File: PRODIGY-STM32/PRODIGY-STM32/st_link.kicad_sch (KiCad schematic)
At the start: 33 parts, among them J3 Conn_ARM_JTAG_SWD_10, Q1 BC850, U1 AP2112K-3.3, U2 STM32F103C8Tx, Y1 8MHz

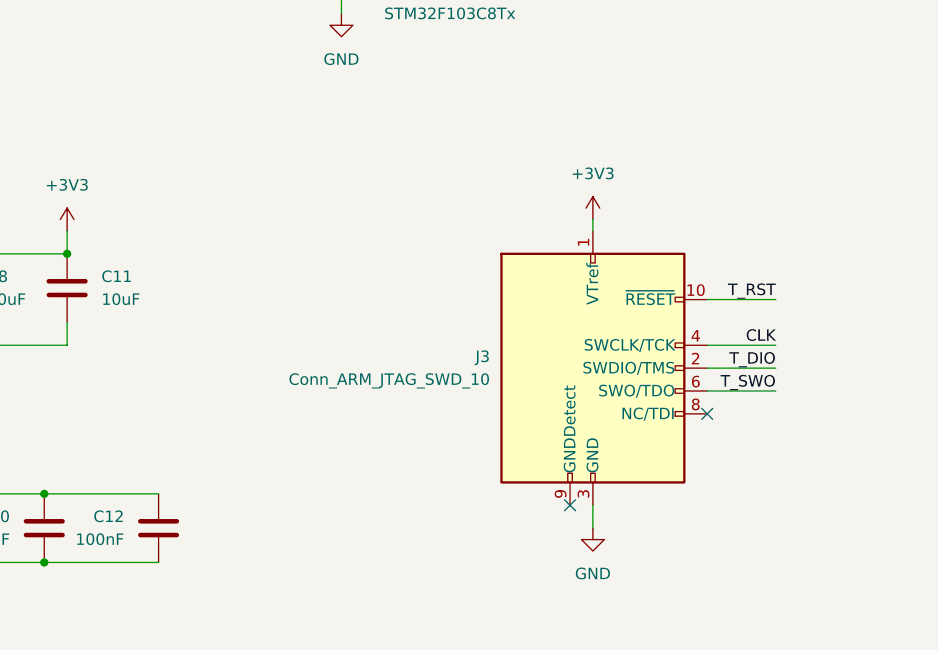
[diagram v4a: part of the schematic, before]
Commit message: stm32 layout done, schematic swd coinnector updated
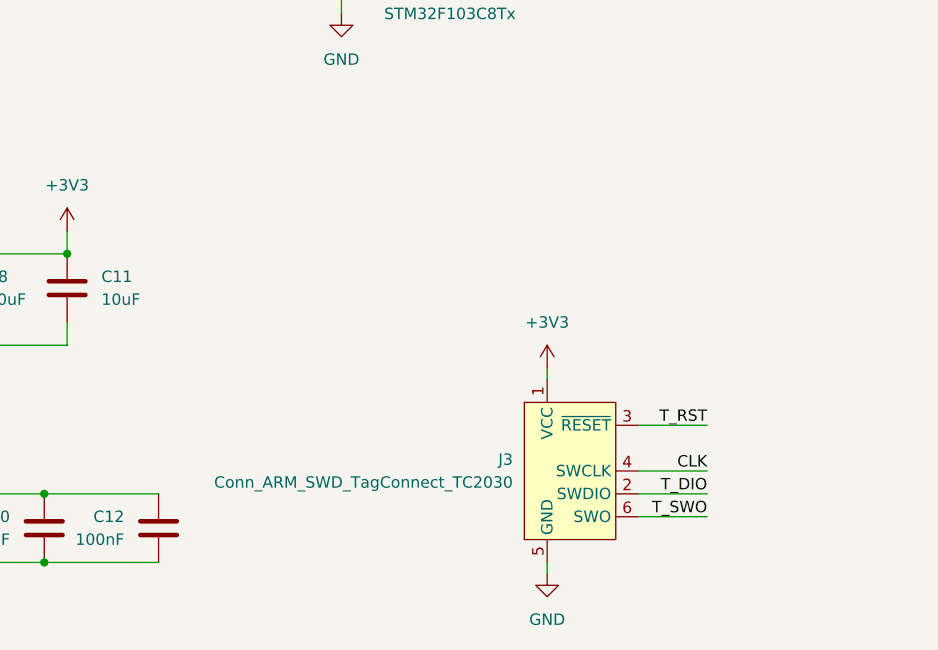
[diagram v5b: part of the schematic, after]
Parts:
- removed J3: Conn_ARM_JTAG_SWD_10, Connector_IDC:IDC-Header_2x05_P2.54mm_Vertical, symbol Connector:Conn_ARM_JTAG_SWD_10
- added J3: Conn_ARM_SWD_TagConnect_TC2030, Connector_PinHeader_2.54mm:PinHeader_1x06_P2.54mm_Vertical, symbol Connector:Conn_ARM_SWD_TagConnect_TC2030
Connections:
- net +3V3: now also J3.1 (VCC)
- net CLK: now also J3.4 (SWCLK)
- net GND: now also J3.5 (GND)
- net T_DIO: now also J3.2 (SWDIO)
- net T_RST: now also J3.3 (~{RESET})
- net T_SWO: now also J3.6 (SWO)
- no-connect marks 20 -> 18

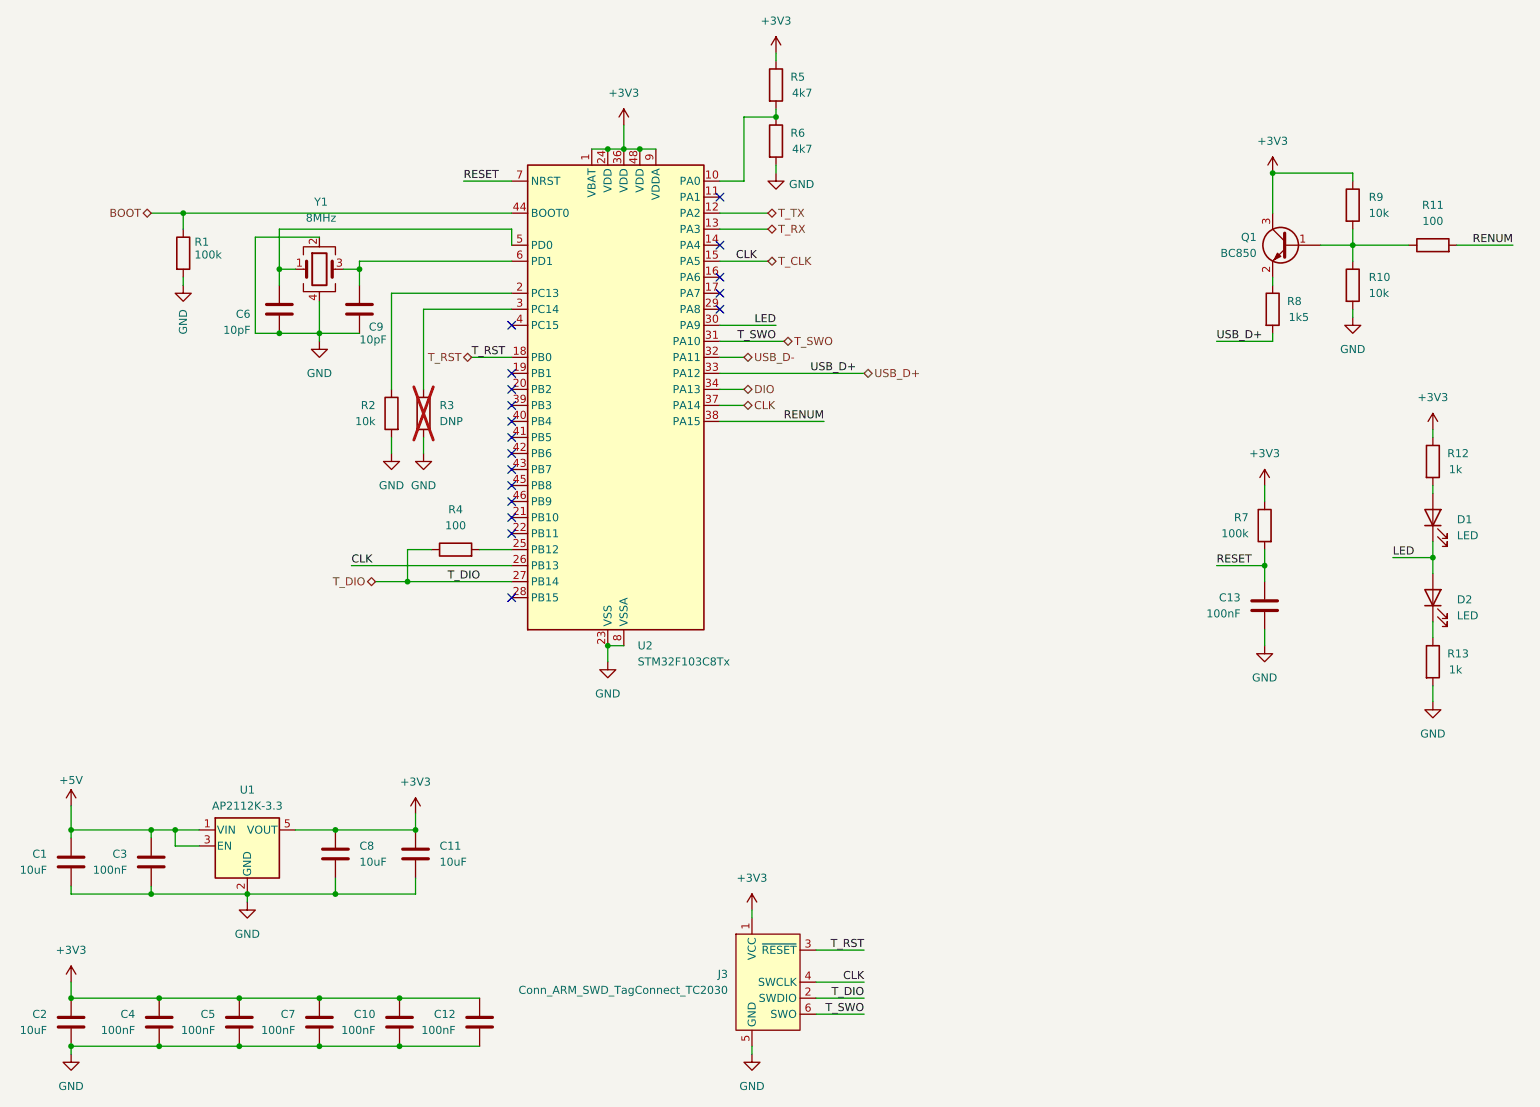
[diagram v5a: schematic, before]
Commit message: stlink wiring done, power vias placed, anlog routing almost done
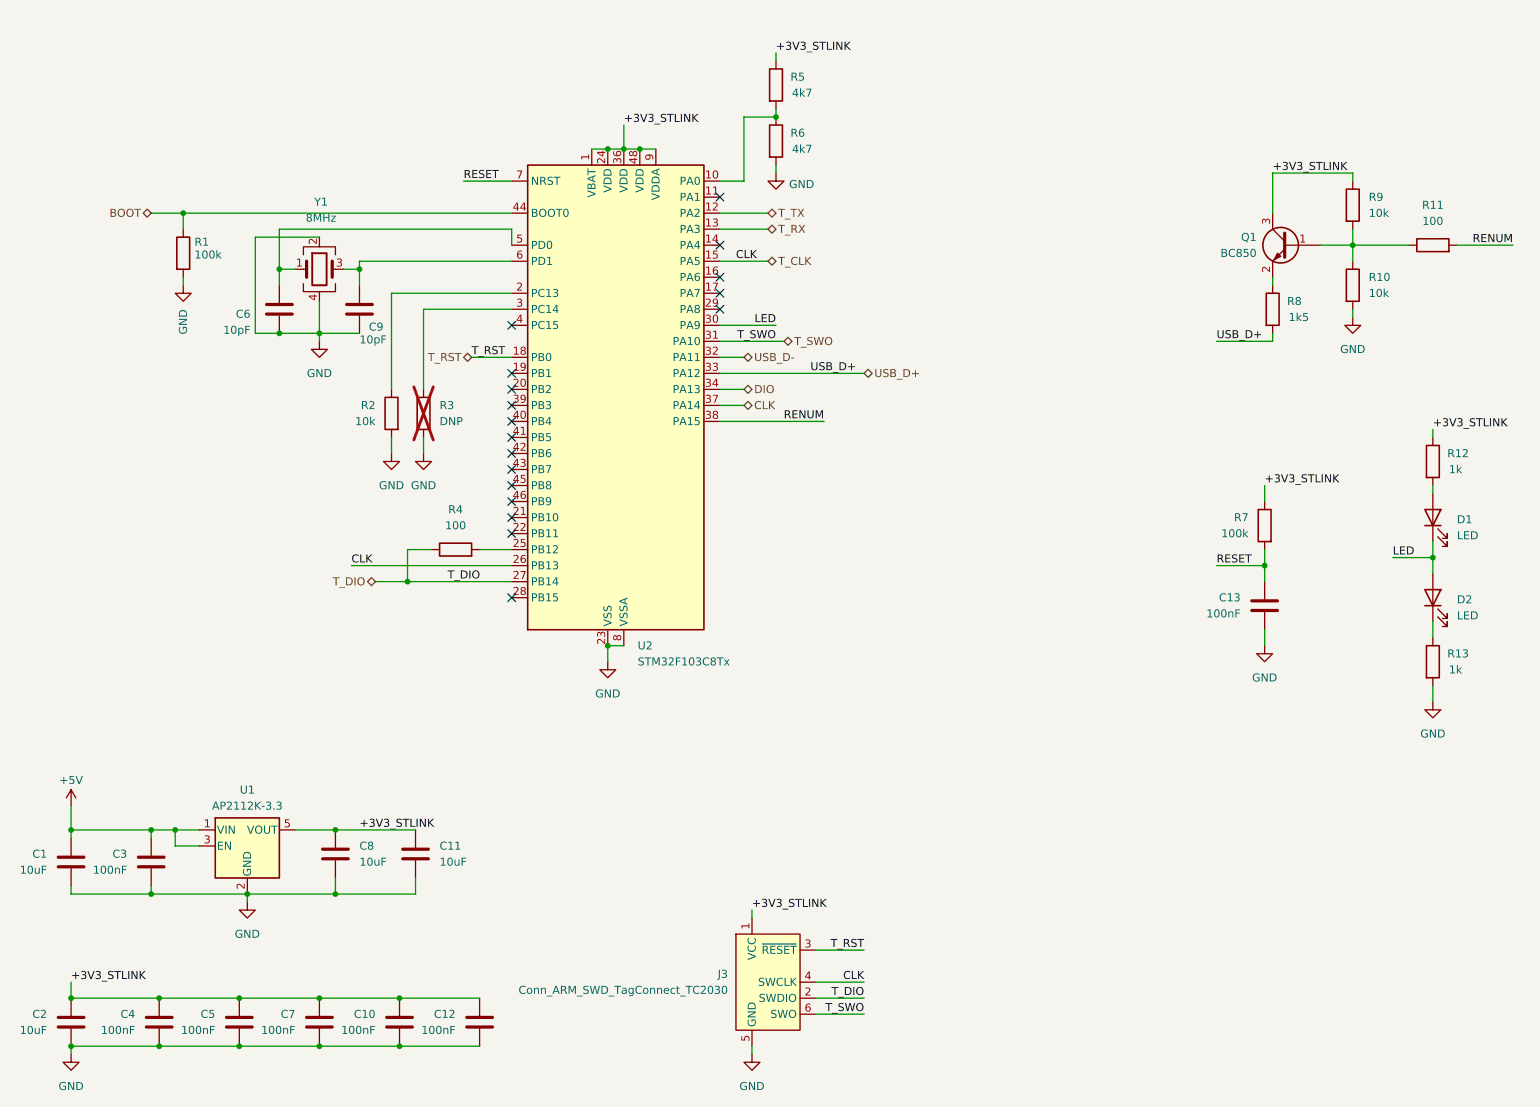
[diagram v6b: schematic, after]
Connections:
- net +3V3 renamed +3V3_STLINK
